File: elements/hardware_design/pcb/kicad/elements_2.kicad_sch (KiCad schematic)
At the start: 36 parts

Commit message: swap wm8731 package (haven't drawn traces yet)
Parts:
- removed IC12: (no value), symbol elements-eagle-import:WM8731
- added U1: WM8731CLSEFL, Package_DFN_QFN:QFN-28-1EP_5x5mm_P0.5mm_EP3.35x3.35mm, symbol Audio:WM8731CLSEFL
- C11, C12: value (none) -> 18p; footprint (none) -> elements:C0603
- C17, C36, C48: value (none) -> 1u; footprint (none) -> elements:C0603
- C18, C21, C22, C33, C34, C38, C39, C46, C47: value (none) -> 100n; footprint (none) -> elements:C0603
- C31, C35: value (none) -> 2.2u; footprint (none) -> elements:C0805
- C52: value (none) -> 10u; footprint (none) -> elements:PANASONIC_B
- F1, F2, F3, F4: value (none) -> FIDUCIAL1X2; footprint (none) -> elements:FIDUCIAL-1X2
- IC10: value (none) -> STM32F405RGT6; footprint (none) -> elements:TQFP-10X10-64
- JP1: value (none) -> M05X2MINIJTAG; footprint (none) -> elements:2X5-1.27
- JP2: value (none) -> M06SIP; footprint (none) -> elements:1X06
- LED1: value (none) -> SSL-LX5093TC; footprint (none) -> elements:LED5MM
- LED2: value (none) -> SSL-LX5093PC; footprint (none) -> elements:LED5MM
- Q1: value (none) -> 8MHz; footprint (none) -> elements:HC49UP
- R44, R47, R52, R53: value (none) -> 2.2k; footprint (none) -> elements:R0603
- R45, R50: value (none) -> 10k; footprint (none) -> elements:R0603
- SW2, SW3: value (none) -> EVQQ2; footprint (none) -> elements:EVQ-Q2
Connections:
- net +3V3: now also U1.3 (DCVDD), U1.5 (DBVDD)
- net +3V3_A: now also U1.12 (HPVDD), U1.18 (AVDD)
- net GND: now also U1.15 (HPGND), U1.19 (AGND), U1.25 (MODE), U1.26 (~{CSB}), U1.29 (AGND), U1.4 (DGND)
- net I2C_SCL: now also R53.1, U1.28 (SCLK); no longer R52.1
- net I2C_SDA: now also R52.1, U1.27 (SDIN); no longer R53.1
- net I2S_LRCK: now also U1.11 (ADCLRC), U1.9 (DACLRC)
- net I2S_MCK: now also U1.1 (XTI/MCLK)
- net I2S_SCK: now also U1.7 (BCLK)
- net I2S_SIN: now also U1.10 (ADCDAT)
- net I2S_SOUT: now also U1.8 (DACDAT)
- net LIN: now also U1.24 (LLINEIN)
- net LOUT: now also U1.16 (LOUT)
- net RIN: now also U1.23 (RLINEIN)
- net ROUT: now also U1.17 (ROUT)
- net at C47.1, C52.+: now also U1.20 (VMID)
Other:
- moved on the sheet: C47, C52, R52, R53

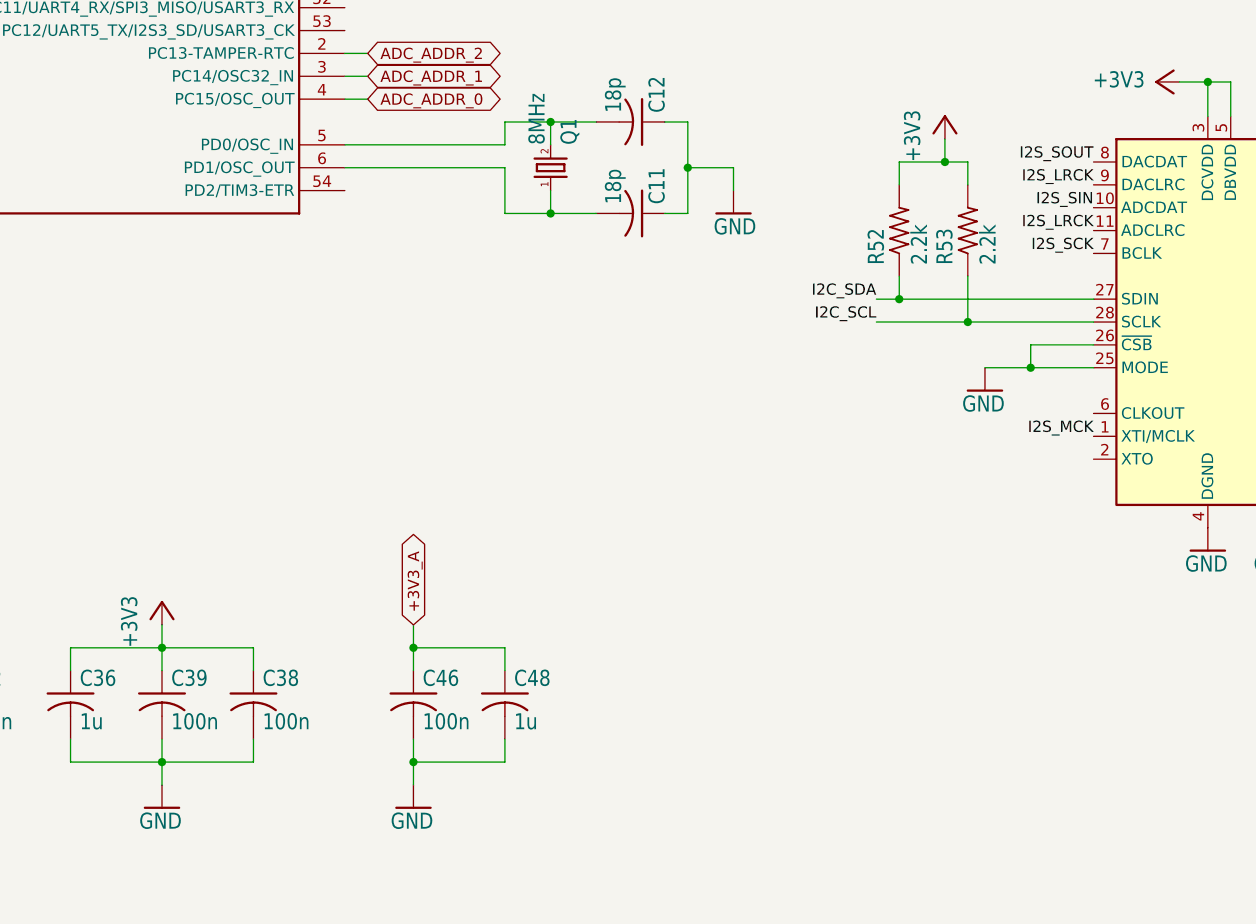
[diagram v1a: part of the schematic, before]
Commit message: traces drawn for wm8731
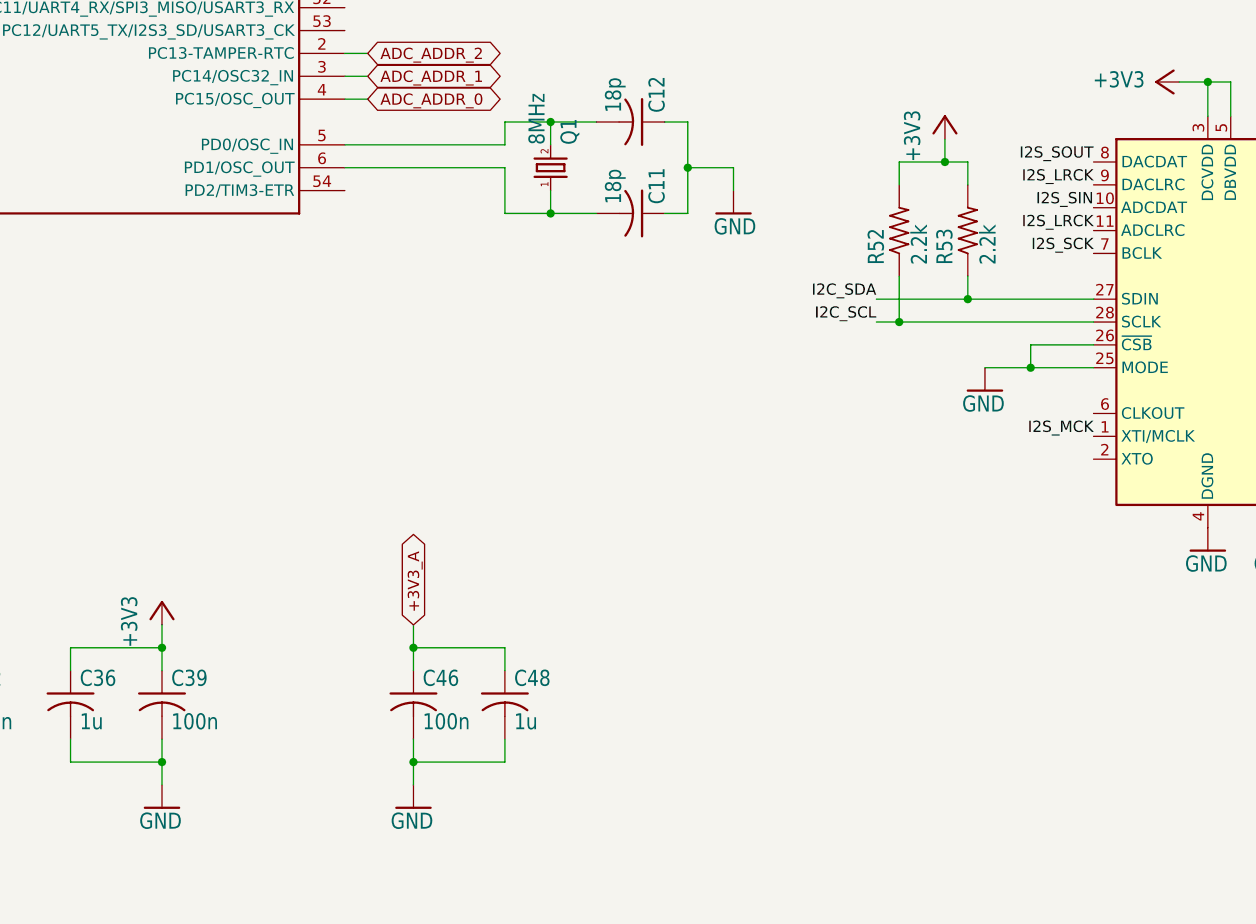
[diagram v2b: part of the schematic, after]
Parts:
- removed C38: 100n, elements:C0603, symbol elements-eagle-import:C-USC0603
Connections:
- net I2C_SCL: now also R52.1; no longer R53.1
- net I2C_SDA: now also R53.1; no longer R52.1
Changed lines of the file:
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@@
   (junction (at 144.78 203.2) (diameter 0) (color 0 0 0 0)
   )
-  (junction (at 313.055 167.005) (diameter 0) (color 0 0 0 0)
-  )
   (junction (at 349.885 140.335) (diameter 0) (color 0 0 0 0)
   )
@@
   (junction (at 266.7 154.94) (diameter 0) (color 0 0 0 0)
   )
+  (junction (at 305.435 167.005) (diameter 0) (color 0 0 0 0)
+  )
+  (junction (at 313.055 164.465) (diameter 0) (color 0 0 0 0)
+  )
   (junction (at 121.92 78.74) (diameter 0) (color 0 0 0 0)
   )
@@
   (junction (at 104.14 106.68) (diameter 0) (color 0 0 0 0)
   )
-  (junction (at 305.435 164.465) (diameter 0) (color 0 0 0 0)
-  )
   (junction (at 266.7 144.78) (diameter 0) (color 0 0 0 0)
   )
@@
     (stroke (width 0) (type default) (color 0 0 0 0))
   )
+  (wire (pts (xy 313.055 161.925) (xy 313.055 164.465))
+    (stroke (width 0) (type default) (color 0 0 0 0))
+  )
   (wire (pts (xy 55.88 99.06) (xy 58.42 99.06))
     (stroke (width 0) (type default) (color 0 0 0 0))
@@
     (stroke (width 0) (type default) (color 0 0 0 0))
   )
-  (wire (pts (xy 302.895 164.465) (xy 305.435 164.465))
+  (wire (pts (xy 302.895 164.465) (xy 313.055 164.465))
     (stroke (width 0) (type default) (color 0 0 0 0))
   )
@@
     (stroke (width 0) (type default) (color 0 0 0 0))
   )
-  (wire (pts (xy 223.52 215.9) (xy 233.68 215.9))
-    (stroke (width 0) (type default) (color 0 0 0 0))
-  )
   (wire (pts (xy 180.34 218.44) (xy 180.34 215.9))
     (stroke (width 0) (type default) (color 0 0 0 0))
@@
     (stroke (width 0) (type default) (color 0 0 0 0))
   )
-  (wire (pts (xy 313.055 167.005) (xy 327.025 167.005))
-    (stroke (width 0) (type default) (color 0 0 0 0))
-  )
   (wire (pts (xy 339.725 140.335) (xy 336.55 140.335))
     (stroke (width 0) (type default) (color 0 0 0 0))
@@
     (stroke (width 0) (type default) (color 0 0 0 0))
   )
+  (wire (pts (xy 313.055 149.225) (xy 313.055 151.765))
+    (stroke (width 0) (type default) (color 0 0 0 0))
+  )
   (wire (pts (xy 213.36 203.2) (xy 223.52 203.2))
     (stroke (width 0) (type default) (color 0 0 0 0))
@@
     (stroke (width 0) (type default) (color 0 0 0 0))
   )
-  (wire (pts (xy 313.055 167.005) (xy 302.895 167.005))
-    (stroke (width 0) (type default) (color 0 0 0 0))
-  )
-  (wire (pts (xy 223.52 203.2) (xy 233.68 203.2))
+  (wire (pts (xy 302.895 167.005) (xy 305.435 167.005))
     (stroke (width 0) (type default) (color 0 0 0 0))
   )
@@
     (stroke (width 0) (type default) (color 0 0 0 0))
   )
-  (wire (pts (xy 313.055 151.765) (xy 313.055 149.225))
-    (stroke (width 0) (type default) (color 0 0 0 0))
-  )
   (wire (pts (xy 40.64 66.04) (xy 38.1 66.04))
     (stroke (width 0) (type default) (color 0 0 0 0))
@@
     (stroke (width 0) (type default) (color 0 0 0 0))
   )
-  (wire (pts (xy 305.435 164.465) (xy 327.025 164.465))
-    (stroke (width 0) (type default) (color 0 0 0 0))
-  )
   (wire (pts (xy 121.92 78.74) (xy 121.92 81.28))
     (stroke (width 0) (type default) (color 0 0 0 0))
   )
+  (wire (pts (xy 305.435 149.225) (xy 305.435 151.765))
+    (stroke (width 0) (type default) (color 0 0 0 0))
+  )
+  (wire (pts (xy 305.435 167.005) (xy 327.025 167.005))
+    (stroke (width 0) (type default) (color 0 0 0 0))
+  )
   (wire (pts (xy 243.84 139.7) (xy 246.38 139.7))
     (stroke (width 0) (type default) (color 0 0 0 0))
@@
     (stroke (width 0) (type default) (color 0 0 0 0))
   )
-  (wire (pts (xy 305.435 161.925) (xy 305.435 164.465))
-    (stroke (width 0) (type default) (color 0 0 0 0))
-  )
   (wire (pts (xy 310.515 149.225) (xy 310.515 146.685))
     (stroke (width 0) (type default) (color 0 0 0 0))
@@
     (stroke (width 0) (type default) (color 0 0 0 0))
   )
+  (wire (pts (xy 313.055 164.465) (xy 327.025 164.465))
+    (stroke (width 0) (type default) (color 0 0 0 0))
+  )
   (wire (pts (xy 349.885 189.865) (xy 349.885 193.675))
     (stroke (width 0) (type default) (color 0 0 0 0))
@@
     (stroke (width 0) (type default) (color 0 0 0 0))
   )
-  (wire (pts (xy 305.435 151.765) (xy 305.435 149.225))
-    (stroke (width 0) (type default) (color 0 0 0 0))
-  )
   (wire (pts (xy 261.62 144.78) (xy 266.7 144.78))
     (stroke (width 0) (type default) (color 0 0 0 0))
@@
     (stroke (width 0) (type default) (color 0 0 0 0))
   )
-  (wire (pts (xy 233.68 205.74) (xy 233.68 203.2))
-    (stroke (width 0) (type default) (color 0 0 0 0))
-  )
   (wire (pts (xy 251.46 203.2) (xy 251.46 200.66))
     (stroke (width 0) (type default) (color 0 0 0 0))
@@
     (stroke (width 0) (type default) (color 0 0 0 0))
   )
+  (wire (pts (xy 305.435 161.925) (xy 305.435 167.005))
+    (stroke (width 0) (type default) (color 0 0 0 0))
+  )
   (wire (pts (xy 251.46 215.9) (xy 251.46 218.44))
     (stroke (width 0) (type default) (color 0 0 0 0))
@@
     (stroke (width 0) (type default) (color 0 0 0 0))
   )
-  (wire (pts (xy 313.055 161.925) (xy 313.055 167.005))
-    (stroke (width 0) (type default) (color 0 0 0 0))
-  )
   (wire (pts (xy 213.36 213.36) (xy 213.36 215.9))
     (stroke (width 0) (type default) (color 0 0 0 0))
@@
   )
   (wire (pts (xy 144.78 215.9) (xy 144.78 218.44))
-    (stroke (width 0) (type default) (color 0 0 0 0))
-  )
-  (wire (pts (xy 233.68 215.9) (xy 233.68 213.36))
     (stroke (width 0) (type default) (color 0 0 0 0))
   )
@@
       (effects (font (size 1.27 1.27)) hide)
     )
-    (pin "1")
-    (pin "2")
-  )
-  (symbol (lib_id "elements-eagle-import:C-USC0603") (at 233.68 208.28 0) (unit 1)
-    (in_bom yes) (on_board yes)
-    (property "Reference" "C38" (id 0) (at 234.696 207.645 0)
-      (effects (font (size 1.778 1.5113)) (justify left bottom))
-    )
-    (property "Value" "100n" (id 1) (at 234.696 212.471 0)
-      (effects (font (size 1.778 1.5113)) (justify left bottom))
-    )
-    (property "Footprint" "elements:C0603" (id 2) (at 233.68 208.28 0)
-      (effects (font (size 1.27 1.27)) hide)
-    )
-    (property "Datasheet" "" (id 3) (at 233.68 208.28 0)
-      (effects (font (size 1.27 1.27)) hide)
-    )

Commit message: smaller boot/reset buttons
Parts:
- SW2, SW3: footprint elements:EVQ-Q2 -> Supercell 1.3:k2-1808 pushbutton switch
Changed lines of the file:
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@@
       (effects (font (size 1.778 1.5113)) (justify left bottom))
     )
-    (property "Footprint" "elements:EVQ-Q2" (id 2) (at 63.5 198.12 0)
+    (property "Footprint" "Supercell 1.3:k2-1808 pushbutton switch" (id 2) (at 63.5 198.12 0)
       (effects (font (size 1.27 1.27)) hide)
     )
@@
       (effects (font (size 1.778 1.5113)) (justify left bottom))
     )
-    (property "Footprint" "elements:EVQ-Q2" (id 2) (at 96.52 210.82 0)
-      (effects (font (size 1.27 1.27)) hide)
-    )
+    (property "Footprint" "Supercell 1.3:k2-1808 pushbutton switch" (id 2) (at 96.52 210.82 0)
+      (effects (font (size 1.27 1.27)) hide)
+    )
